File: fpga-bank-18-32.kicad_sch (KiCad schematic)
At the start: 1 part, among them U1 XC7K410T-2FFG900I

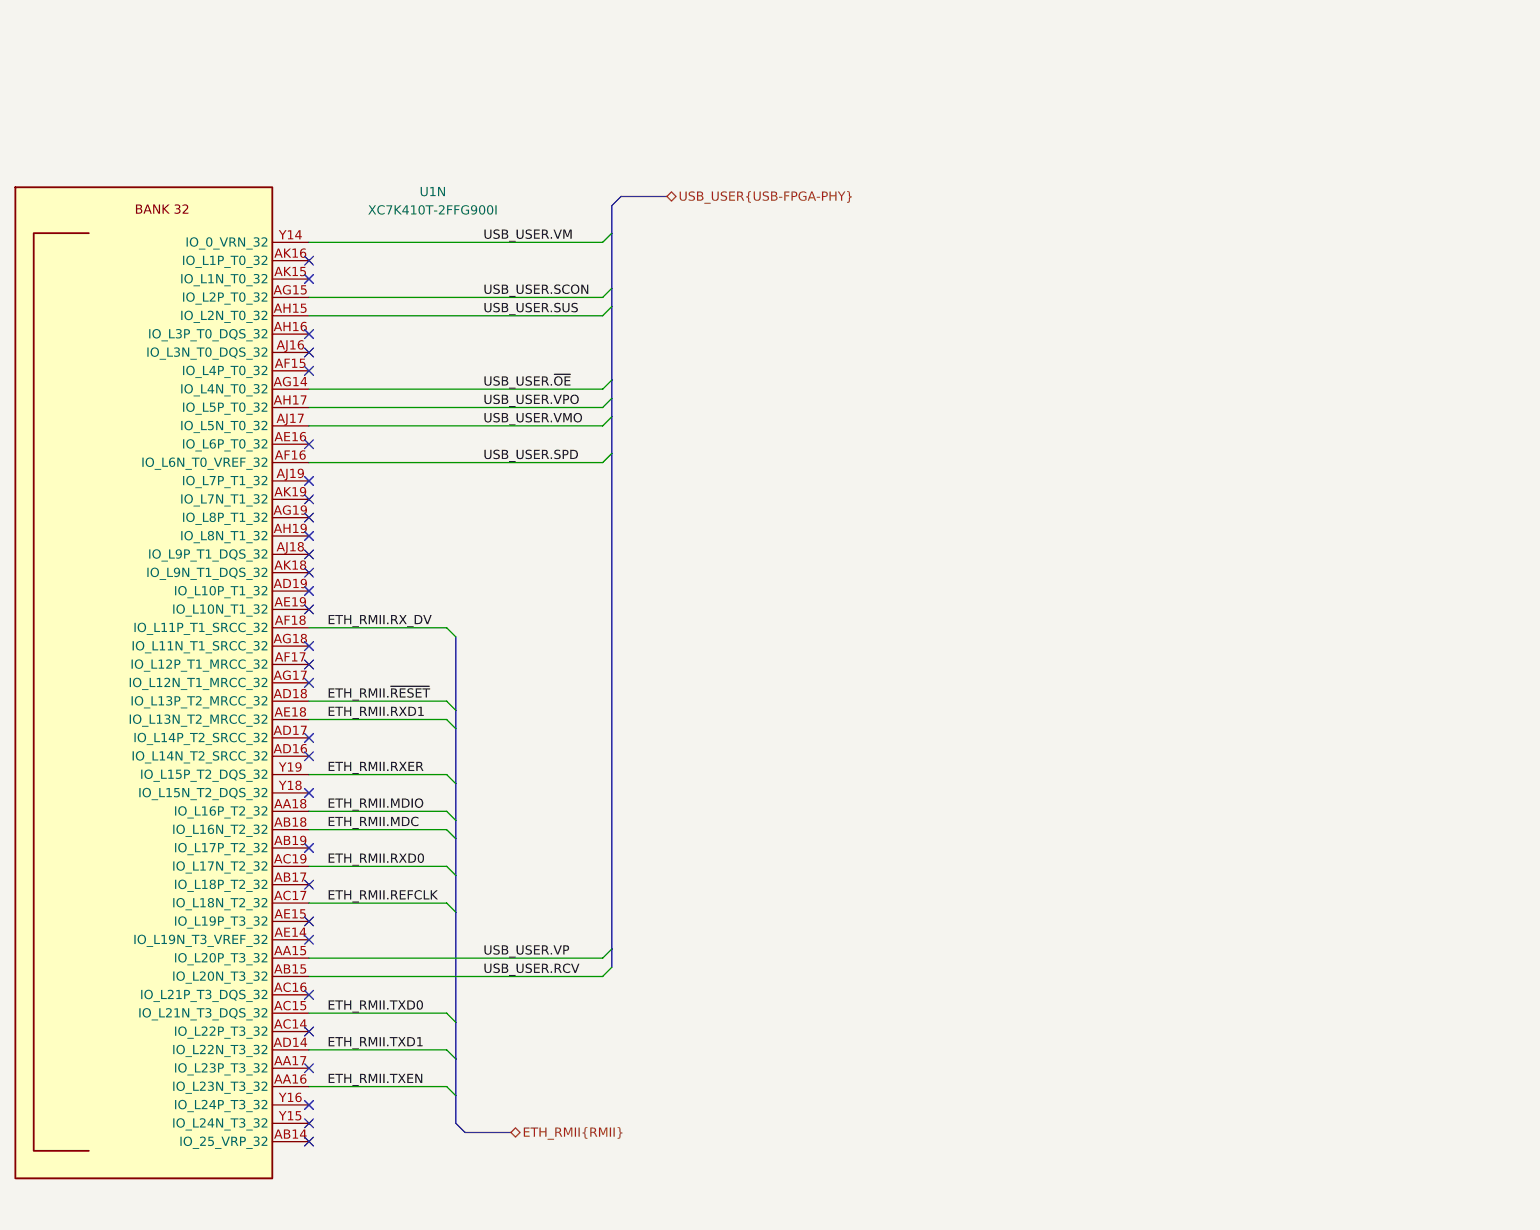
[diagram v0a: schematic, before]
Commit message: [#55729] Switch FPGA symbol to antmicroFPGAChips lib
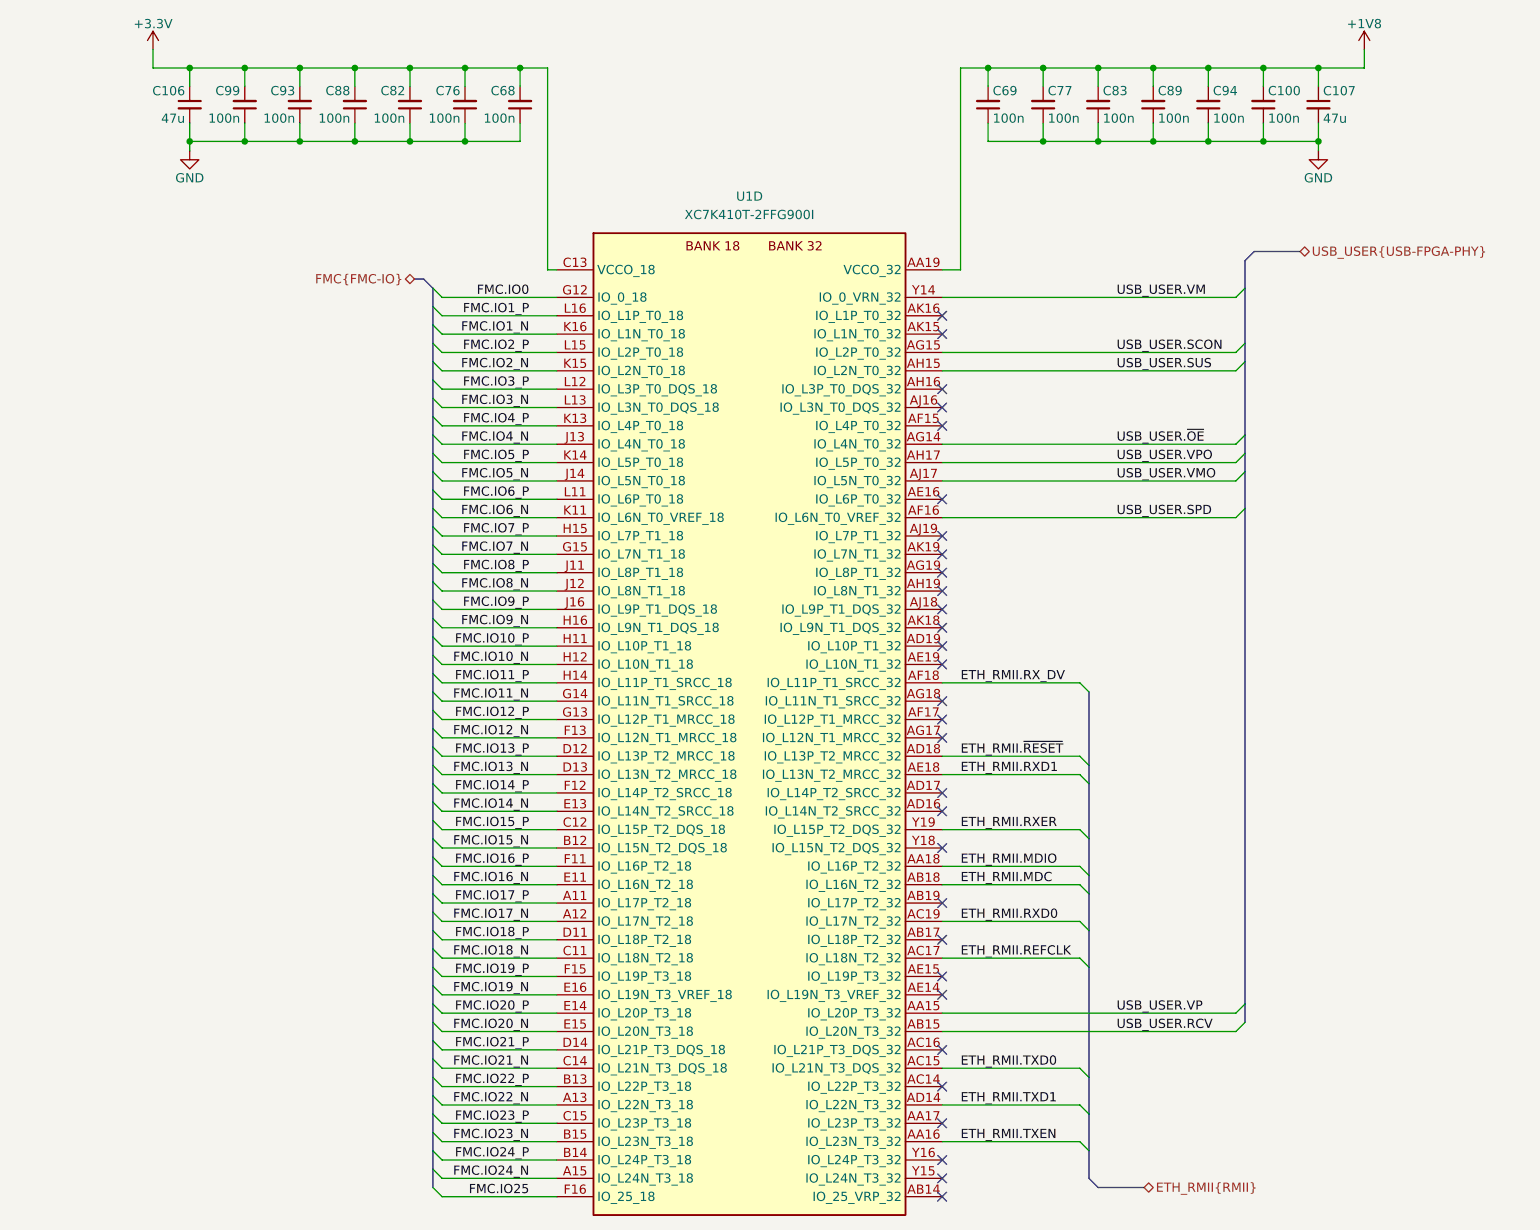
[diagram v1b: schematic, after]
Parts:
- added C100, C68, C69, C76, C77, C82, C83, C88, C89, C93, C94, C99: C_100n_0402, antmicro-footprints:C_0402_1005Metric, symbol antmicroCapacitors0402:C_100n_0402
- added C106, C107: C_47u_0603, antmicro-footprints:C_0603_1608Metric, symbol antmicroCapacitors0603:C_47u_0603
- U1: footprint K410T-devboard-footprints:xc7k410t-2ffg900I -> antmicro-footprints:BGA-900_31x31mm_Layout30x30_P1x1mm_FFG900; symbol K410T-devboard:XC7K410T-2FFG900I -> antmicroFPGAChips:XC7K410T-2FFG900I
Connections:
- new net +1V8: C100.2, C107.1, C69.2, C77.2, C83.2, C89.2, C94.2, U1.AA19 (VCCO_32), U1.AB16 (VCCO_32), U1.AE17 (VCCO_32), U1.AF14 (VCCO_32), U1.AH18 (VCCO_32), U1.AJ15 (VCCO_32)
- new net +3V3: C106.1, C68.2, C76.2, C82.2, C88.2, C93.2, C99.2, U1.C13 (VCCO_18), U1.D10 (VCCO_18), U1.F14 (VCCO_18), U1.G11 (VCCO_18), U1.J15 (VCCO_18), U1.K12 (VCCO_18)
- new net FMC.IO0: U1.G12 (IO_0_18)
- new net FMC.IO10_N: U1.H12 (IO_L10N_T1_18)
- new net FMC.IO10_P: U1.H11 (IO_L10P_T1_18)
- new net FMC.IO11_N: U1.G14 (IO_L11N_T1_SRCC_18)
- new net FMC.IO11_P: U1.H14 (IO_L11P_T1_SRCC_18)
- new net FMC.IO12_N: U1.F13 (IO_L12N_T1_MRCC_18)
- new net FMC.IO12_P: U1.G13 (IO_L12P_T1_MRCC_18)
- new net FMC.IO13_N: U1.D13 (IO_L13N_T2_MRCC_18)
- new net FMC.IO13_P: U1.D12 (IO_L13P_T2_MRCC_18)
- new net FMC.IO14_N: U1.E13 (IO_L14N_T2_SRCC_18)
- new net FMC.IO14_P: U1.F12 (IO_L14P_T2_SRCC_18)
- new net FMC.IO15_N: U1.B12 (IO_L15N_T2_DQS_18)
- new net FMC.IO15_P: U1.C12 (IO_L15P_T2_DQS_18)
- new net FMC.IO16_N: U1.E11 (IO_L16N_T2_18)
- new net FMC.IO16_P: U1.F11 (IO_L16P_T2_18)
- new net FMC.IO17_N: U1.A12 (IO_L17N_T2_18)
- new net FMC.IO17_P: U1.A11 (IO_L17P_T2_18)
- new net FMC.IO18_N: U1.C11 (IO_L18N_T2_18)
- new net FMC.IO18_P: U1.D11 (IO_L18P_T2_18)
- new net FMC.IO19_N: U1.E16 (IO_L19N_T3_VREF_18)
- new net FMC.IO19_P: U1.F15 (IO_L19P_T3_18)
- new net FMC.IO1_N: U1.K16 (IO_L1N_T0_18)
- new net FMC.IO1_P: U1.L16 (IO_L1P_T0_18)
- new net FMC.IO20_N: U1.E15 (IO_L20N_T3_18)
- new net FMC.IO20_P: U1.E14 (IO_L20P_T3_18)
- new net FMC.IO21_N: U1.C14 (IO_L21N_T3_DQS_18)
- new net FMC.IO21_P: U1.D14 (IO_L21P_T3_DQS_18)
- new net FMC.IO22_N: U1.A13 (IO_L22N_T3_18)
- new net FMC.IO22_P: U1.B13 (IO_L22P_T3_18)
- new net FMC.IO23_N: U1.B15 (IO_L23N_T3_18)
- new net FMC.IO23_P: U1.C15 (IO_L23P_T3_18)
- new net FMC.IO24_N: U1.A15 (IO_L24N_T3_18)
- new net FMC.IO24_P: U1.B14 (IO_L24P_T3_18)
- new net FMC.IO25: U1.F16 (IO_25_18)
- new net FMC.IO2_N: U1.K15 (IO_L2N_T0_18)
- new net FMC.IO2_P: U1.L15 (IO_L2P_T0_18)
- new net FMC.IO3_N: U1.L13 (IO_L3N_T0_DQS_18)
- new net FMC.IO3_P: U1.L12 (IO_L3P_T0_DQS_18)
- new net FMC.IO4_N: U1.J13 (IO_L4N_T0_18)
- new net FMC.IO4_P: U1.K13 (IO_L4P_T0_18)
- new net FMC.IO5_N: U1.J14 (IO_L5N_T0_18)
- new net FMC.IO5_P: U1.K14 (IO_L5P_T0_18)
- new net FMC.IO6_N: U1.K11 (IO_L6N_T0_VREF_18)
- new net FMC.IO6_P: U1.L11 (IO_L6P_T0_18)
- new net FMC.IO7_N: U1.G15 (IO_L7N_T1_18)
- new net FMC.IO7_P: U1.H15 (IO_L7P_T1_18)
- new net FMC.IO8_N: U1.J12 (IO_L8N_T1_18)
- new net FMC.IO8_P: U1.J11 (IO_L8P_T1_18)
- new net FMC.IO9_N: U1.H16 (IO_L9N_T1_DQS_18)
- new net FMC.IO9_P: U1.J16 (IO_L9P_T1_DQS_18)
- new net GND: C100.1, C106.2, C107.2, C68.1, C69.1, C76.1, C77.1, C82.1, C83.1, C88.1, C89.1, C93.1, C94.1, C99.1

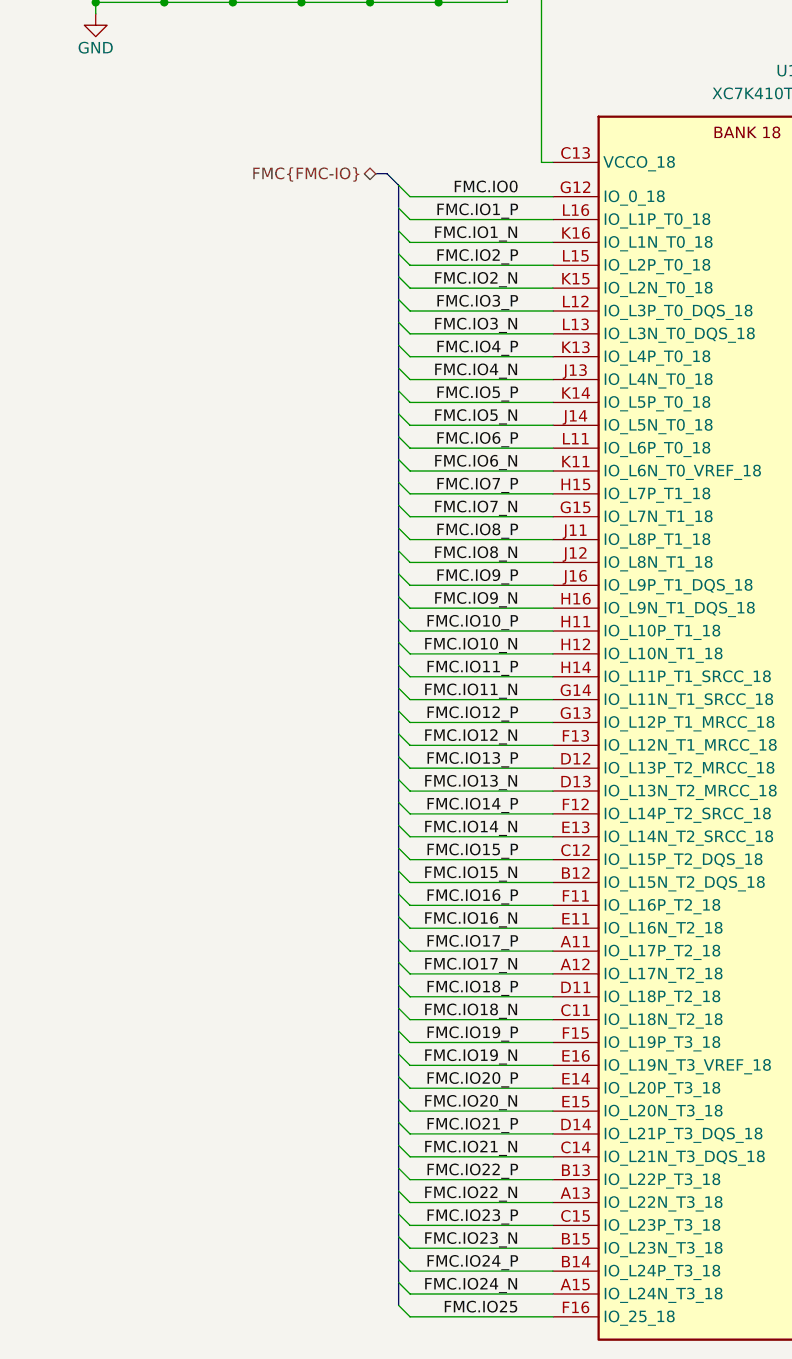
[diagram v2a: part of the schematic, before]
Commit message: [#55729] Clean schematics/update from lib
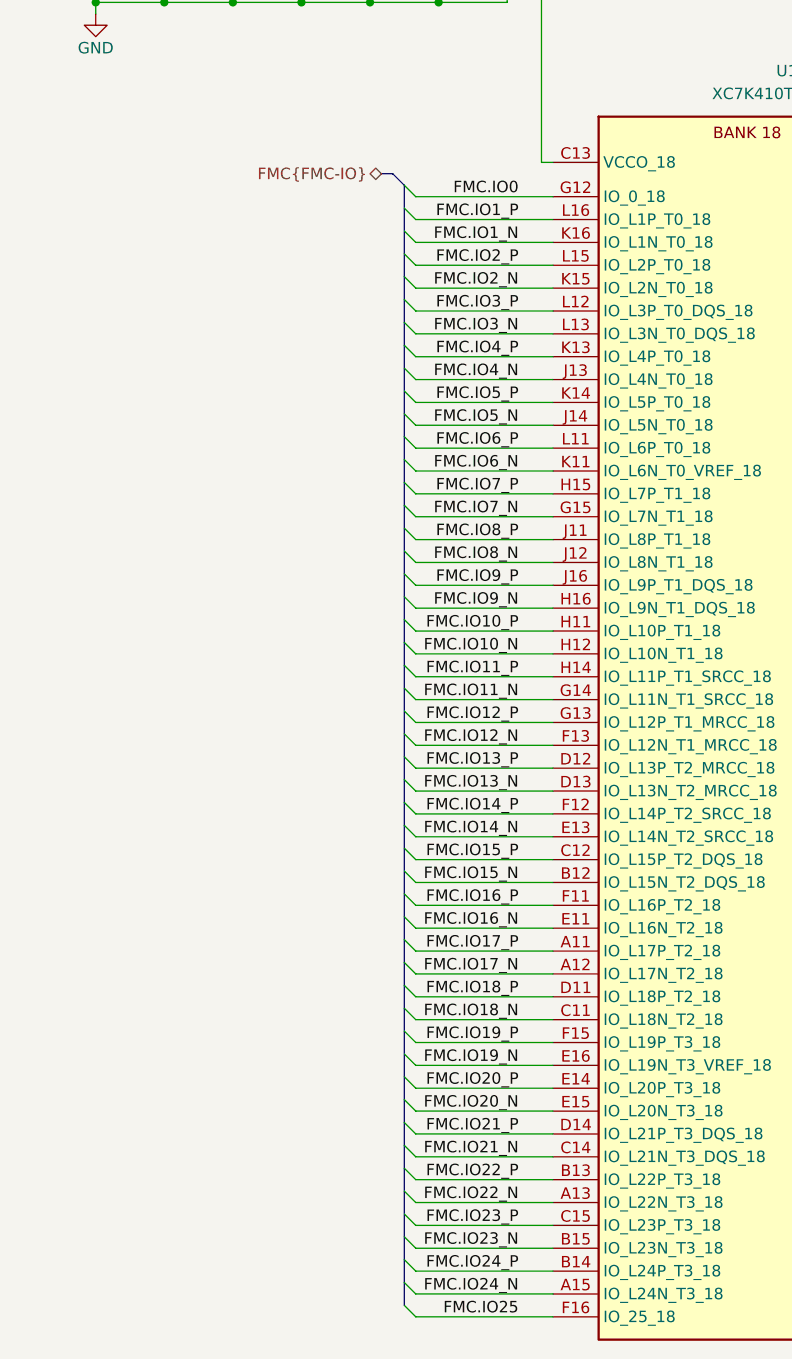
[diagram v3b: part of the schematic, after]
